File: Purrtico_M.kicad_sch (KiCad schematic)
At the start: 119 parts, among them J1 Conn_02x05_Odd_Even, J2 Conn_01x02, J4 Conn_01x02, U1 OPA1679, U2 OPA1679, U3 OPA1679

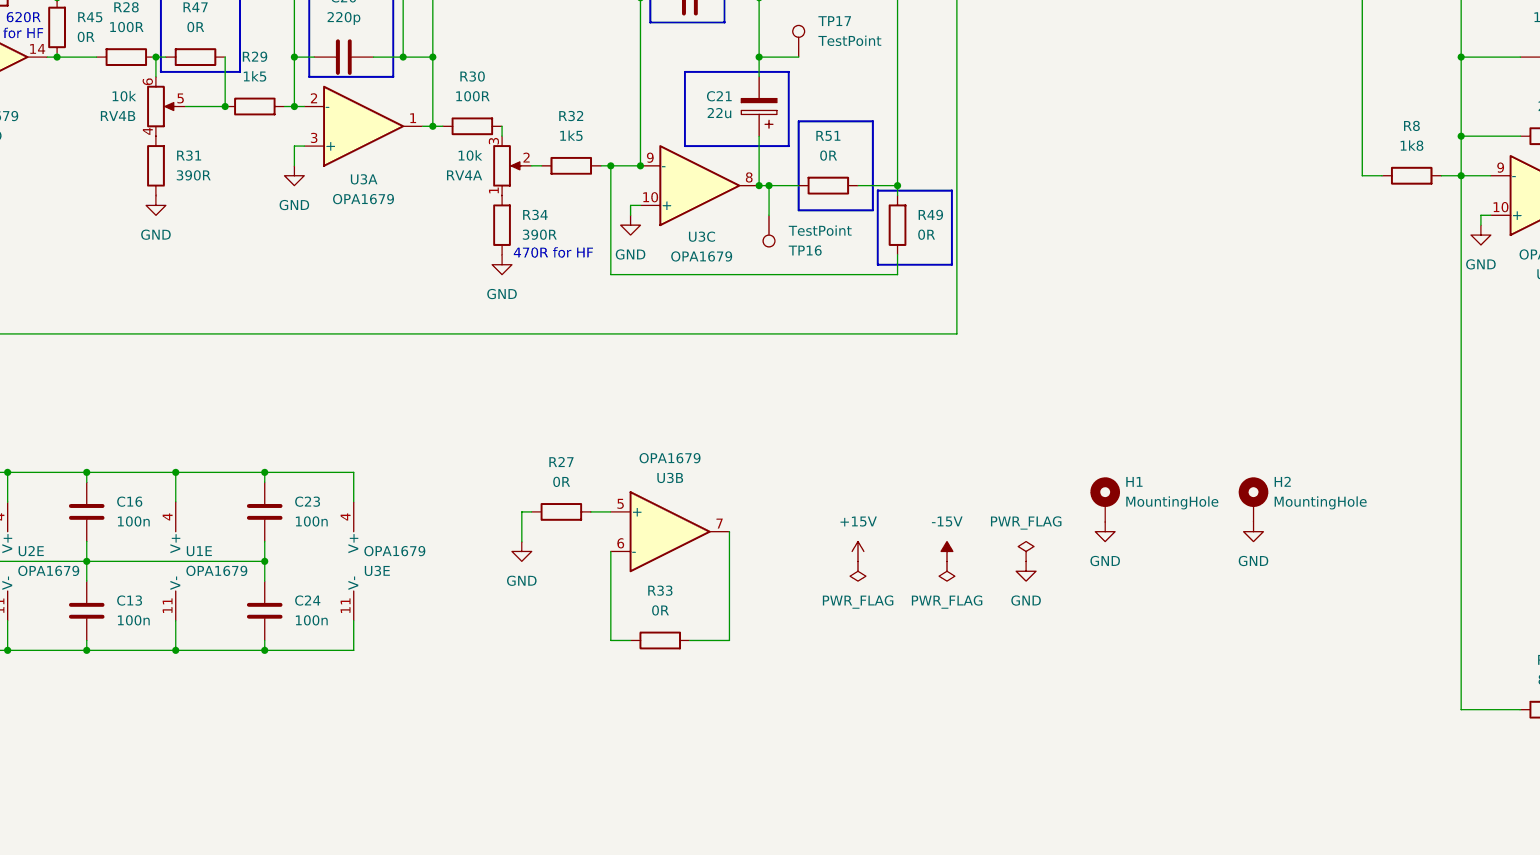
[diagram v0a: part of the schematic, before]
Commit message: added input gain control
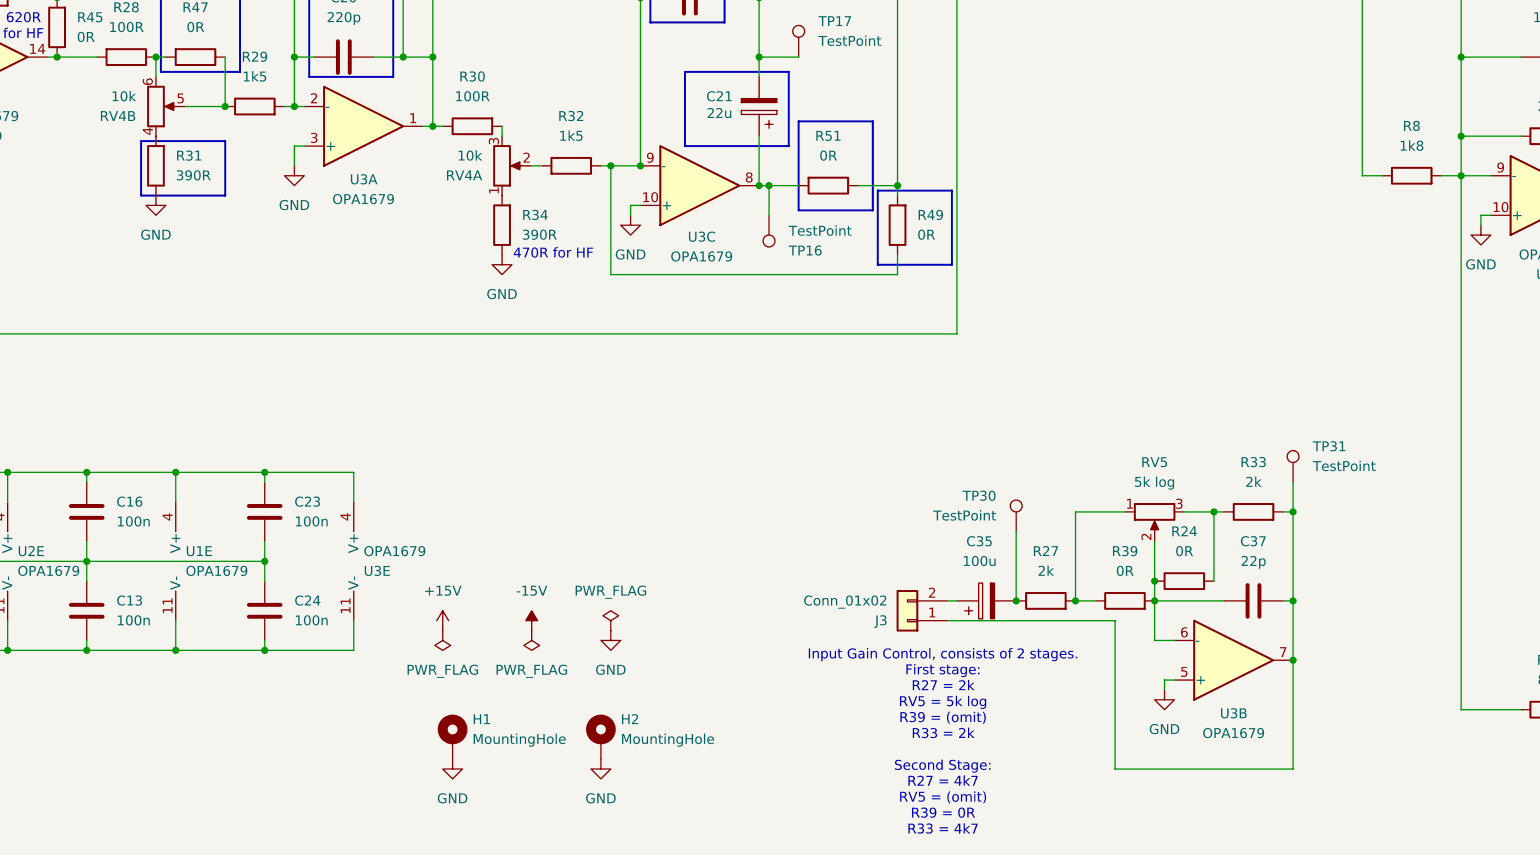
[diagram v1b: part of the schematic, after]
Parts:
- added C35: 100u, Capacitor_THT:CP_Radial_D6.3mm_P2.50mm, symbol Device:C_Polarized
- added C37: 22p, Capacitor_SMD:C_1206_3216Metric, symbol Device:C
- added J3: Conn_01x02, Connector_PinHeader_2.54mm:PinHeader_1x02_P2.54mm_Vertical, symbol Connector_Generic:Conn_01x02
- added R24, R39: 0R, Resistor_SMD:R_1206_3216Metric, symbol Device:R
- added RV5: 5k log, Connector_PinHeader_2.54mm:PinHeader_1x03_P2.54mm_Vertical, symbol Device:R_Potentiometer
- added TP30, TP31: TestPoint, TestPoint:TestPoint_THTPad_D1.0mm_Drill0.5mm, symbol Connector:TestPoint
- R27, R33: value 0R -> 2k
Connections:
- net GND: now also U3.5 (+); no longer R27.1
- net at R27.2: now also R39.1, RV5.1; no longer U3.5 (+)
- net at U3.6 (-): now also C37.2, R24.1, R39.2, RV5.2; no longer R33.1
- net at R33.2, U3.7: now also C37.1, J3.1 (Pin_1), TP31.1
- new net: R24.2, R33.1, RV5.3
- new net: C35.2, R27.1, TP30.1
- new net: C35.1, J3.2 (Pin_2)
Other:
- note added: "Input Gain Control, consists of 2 stages. First stage: R27 = 2k RV5 = 5k log R39 = (omit) R33 = 2k Second Stage: R27 = 4k7 RV5 = (omit) R39 = 0R R33 = 4k7"
- moved on the sheet: H1, H2, R27, R33, U3B

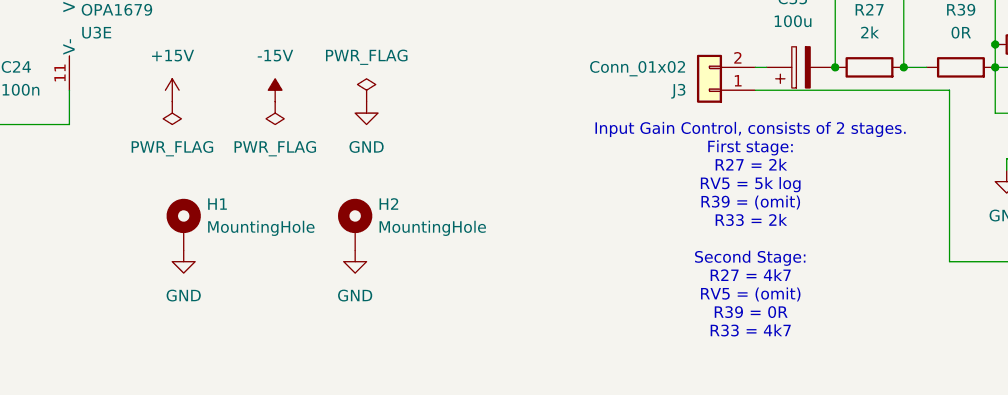
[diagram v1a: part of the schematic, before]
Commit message: added 0R for mounting holes
as well as some small layout refinements
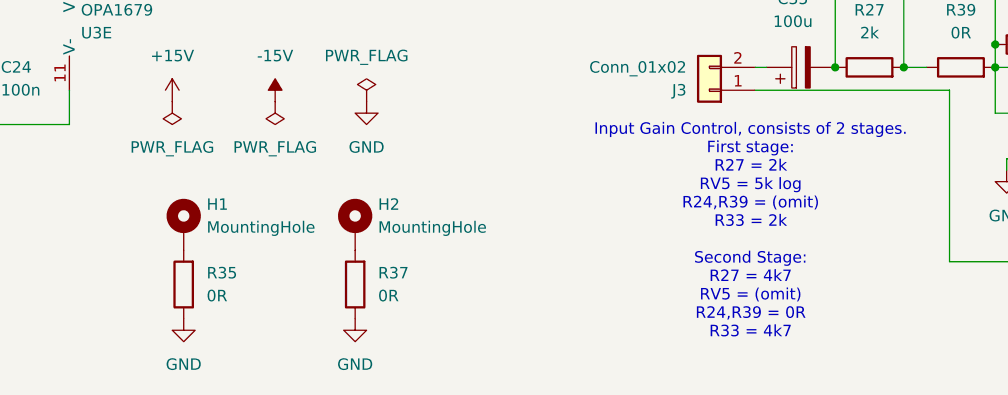
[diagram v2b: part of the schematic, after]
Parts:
- added R35, R37: 0R, Resistor_SMD:R_1206_3216Metric, symbol Device:R
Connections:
- net GND: now also R35.1, R37.1; no longer H1.1, H2.1
- new net: H2.1, R37.2
- new net: H1.1, R35.2
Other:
- note added: "Input Gain Control, consists of 2 stages. First stage: R27 = 2k RV5 = 5k log R24,R39 = (omit) R33 = 2k Second Stage: R27 = 4k7 RV5 = (omit) R24,R39 = 0R R33 = 4k7"
- note removed: "Input Gain Control, consists of 2 stages. First stage: R27 = 2k RV5 = 5k log R39 = (omit) R33 = 2k Second Stage: R27 = 4k7 RV5 = (omit) R39 = 0R R33 = 4k7"
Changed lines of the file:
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@@
 	(title_block
 		(title "Purrtico M")
-		(date "2024-08-06")
+		(date "2024-08-14")
 		(rev "01")
 		(company "Greybox Audio")
@@
 		)
 	)
-	(text "Input Gain Control, consists of 2 stages.\nFirst stage:\nR27 = 2k\nRV5 = 5k log\nR39 = (omit)\nR33 = 2k\n\nSecond Stage:\nR27 = 4k7\nRV5 = (omit)\nR39 = 0R\nR33 = 4k7"
+	(text "Input Gain Control, consists of 2 stages.\nFirst stage:\nR27 = 2k\nRV5 = 5k log\nR24,R39 = (omit)\nR33 = 2k\n\nSecond Stage:\nR27 = 4k7\nRV5 = (omit)\nR24,R39 = 0R\nR33 = 4k7"
 		(exclude_from_sim no)
 		(at 212.852 210.058 0)
@@
 	)
 	(symbol
+		(lib_id "Device:R")
+		(at 149.86 215.9 180)
+		(unit 1)
+		(exclude_from_sim no)
+		(in_bom yes)
+		(on_board yes)
+		(dnp no)
+		(fields_autoplaced yes)
+		(property "Reference" "R35"
+			(at 152.4 214.6299 0)
+			(effects
+				(font
+					(size 1.27 1.27)
+				)
+				(justify right)
+			)
+		)
+		(property "Value" "0R"
+			(at 152.4 217.1699 0)
+			(effects
+				(font
+					(size 1.27 1.27)
+				)
+				(justify right)
+			)
+		)
+		(property "Footprint" "Resistor_SMD:R_1206_3216Metric"
+			(at 151.638 215.9 90)
+			(effects
+				(font
+					(size 1.27 1.27)
+				)
+				(hide yes)
+			)
+		)
+		(property "Datasheet" "~"
+			(at 149.86 215.9 0)
+			(effects
+				(font
+					(size 1.27 1.27)
+				)
+				(hide yes)
+			)
+		)
+		(property "Description" "Resistor"
+			(at 149.86 215.9 0)
+			(effects
+				(font
+					(size 1.27 1.27)
+				)
+				(hide yes)
+			)
+		)
+		(pin "2"
+		)
+		(pin "1"
+		)
+		(instances
+			(project "Purrtico_M"
+				(path "/a0898129-0e9a-4d09-a24b-7ec1243d6ca2"
+					(reference "R35")
+					(unit 1)
+				)
+			)
+		)
+	)
+	(symbol
 		(lib_id "Device:C")
 		(at 177.8 44.45 90)
@@
 	(symbol
 		(lib_id "Device:R")
+		(at 168.91 215.9 180)
+		(unit 1)
+		(exclude_from_sim no)
+		(in_bom yes)
+		(on_board yes)
+		(dnp no)
+		(fields_autoplaced yes)
+		(property "Reference" "R37"
+			(at 171.45 214.6299 0)
+			(effects
+				(font
+					(size 1.27 1.27)
+				)
+				(justify right)
+			)
+		)
+		(property "Value" "0R"
+			(at 171.45 217.1699 0)
+			(effects
+				(font
+					(size 1.27 1.27)
+				)
+				(justify right)
+			)
+		)
+		(property "Footprint" "Resistor_SMD:R_1206_3216Metric"
+			(at 170.688 215.9 90)
+			(effects
+				(font
+					(size 1.27 1.27)
+				)
+				(hide yes)
+			)
+		)
+		(property "Datasheet" "~"
+			(at 168.91 215.9 0)
+			(effects
+				(font
+					(size 1.27 1.27)
+				)
+				(hide yes)
+			)
+		)
+		(property "Description" "Resistor"
+			(at 168.91 215.9 0)
+			(effects
+				(font
+					(size 1.27 1.27)
+				)
+				(hide yes)
+			)
+		)
+		(pin "2"
+		)
+		(pin "1"
+		)
+		(instances
+			(project "Purrtico_M"
+				(path "/a0898129-0e9a-4d09-a24b-7ec1243d6ca2"
+					(reference "R37")
+					(unit 1)
+				)
+			)
+		)
+	)
+	(symbol
+		(lib_id "Device:R")
 		(at 337.82 59.69 90)
 		(unit 1)
@@
 		(lib_name "GND_1")
 		(lib_id "power:GND")
-		(at 149.86 212.09 0)
+		(at 149.86 219.71 0)
 		(unit 1)
 		(exclude_from_sim no)
@@
 		(fields_autoplaced yes)
 		(property "Reference" "#PWR011"
-			(at 149.86 218.44 0)
+			(at 149.86 226.06 0)
 			(effects
 				(font
@@
 		)
 		(property "Value" "GND"
-			(at 149.86 217.17 0)
+			(at 149.86 224.79 0)
 			(effects
 				(font
@@
 		)
 		(property "Footprint" ""
-			(at 149.86 212.09 0)
+			(at 149.86 219.71 0)
 			(effects
 				(font
@@
 		)
 		(property "Datasheet" ""
-			(at 149.86 212.09 0)
+			(at 149.86 219.71 0)
 			(effects
 				(font
@@
 		)
 		(property "Description" "Power symbol creates a global label with name \"GND\" , ground"
-			(at 149.86 212.09 0)
+			(at 149.86 219.71 0)
 			(effects
 				(font
@@
 		(lib_name "GND_1")
 		(lib_id "power:GND")
-		(at 168.91 212.09 0)
+		(at 168.91 219.71 0)
 		(unit 1)
 		(exclude_from_sim no)
@@
 		(fields_autoplaced yes)
 		(property "Reference" "#PWR012"
-			(at 168.91 218.44 0)
+			(at 168.91 226.06 0)
 			(effects
 				(font
@@
 		)
 		(property "Value" "GND"
-			(at 168.91 217.17 0)
+			(at 168.91 224.79 0)
 			(effects
 				(font
@@
 		)
 		(property "Footprint" ""
-			(at 168.91 212.09 0)
+			(at 168.91 219.71 0)
 			(effects
 				(font
@@
 		)
 		(property "Datasheet" ""
-			(at 168.91 212.09 0)
+			(at 168.91 219.71 0)
 			(effects
 				(font
@@
 		)
 		(property "Description" "Power symbol creates a global label with name \"GND\" , ground"
-			(at 168.91 212.09 0)
+			(at 168.91 219.71 0)
 			(effects
 				(font

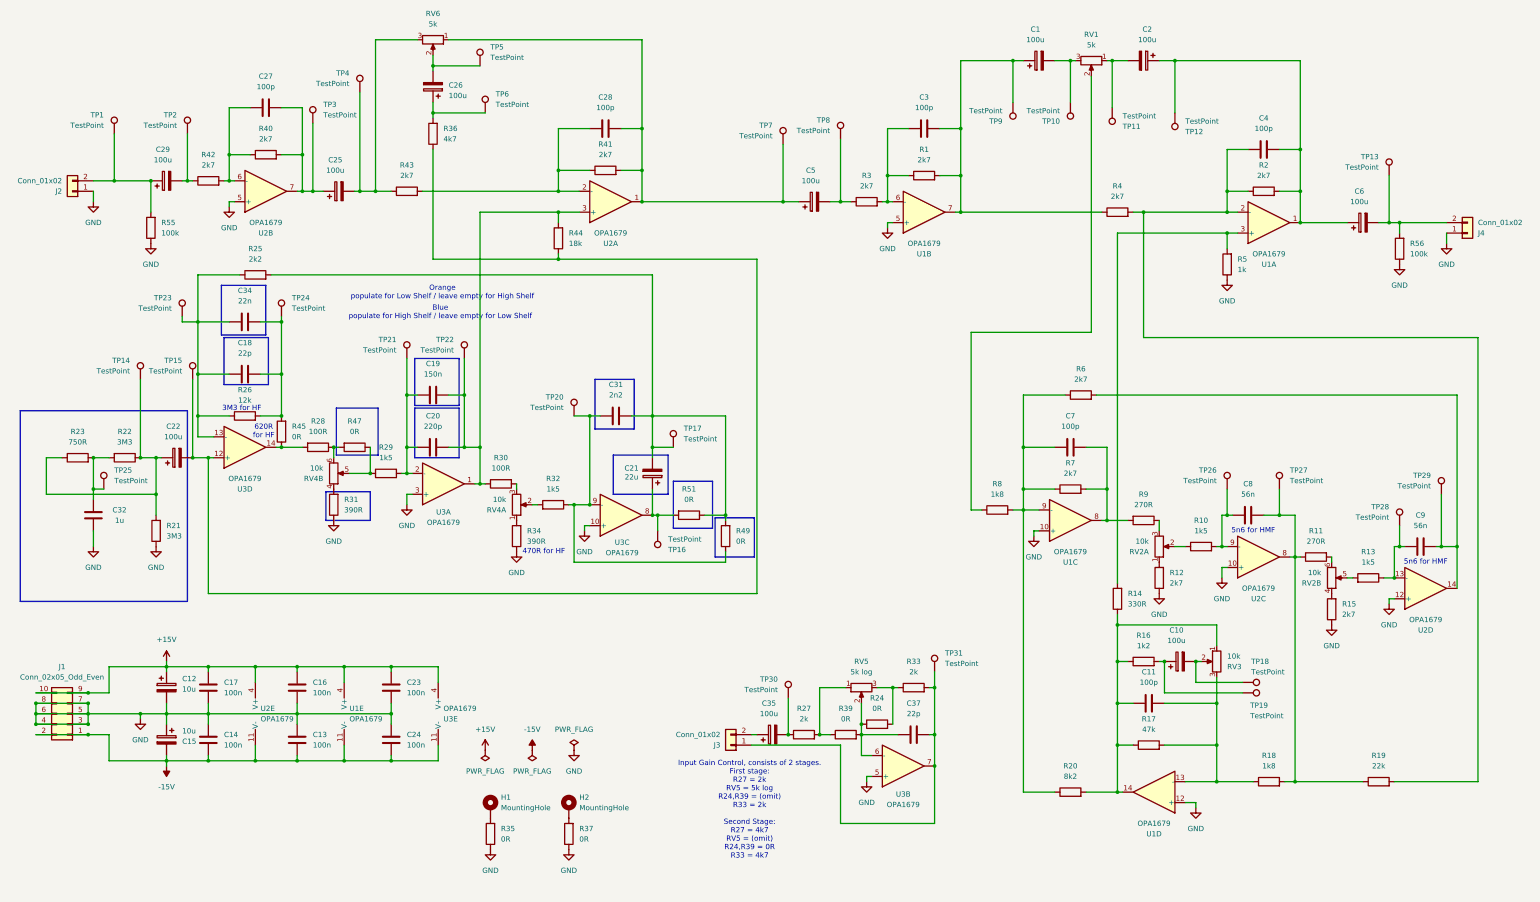
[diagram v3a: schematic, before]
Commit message: update potentiometer values
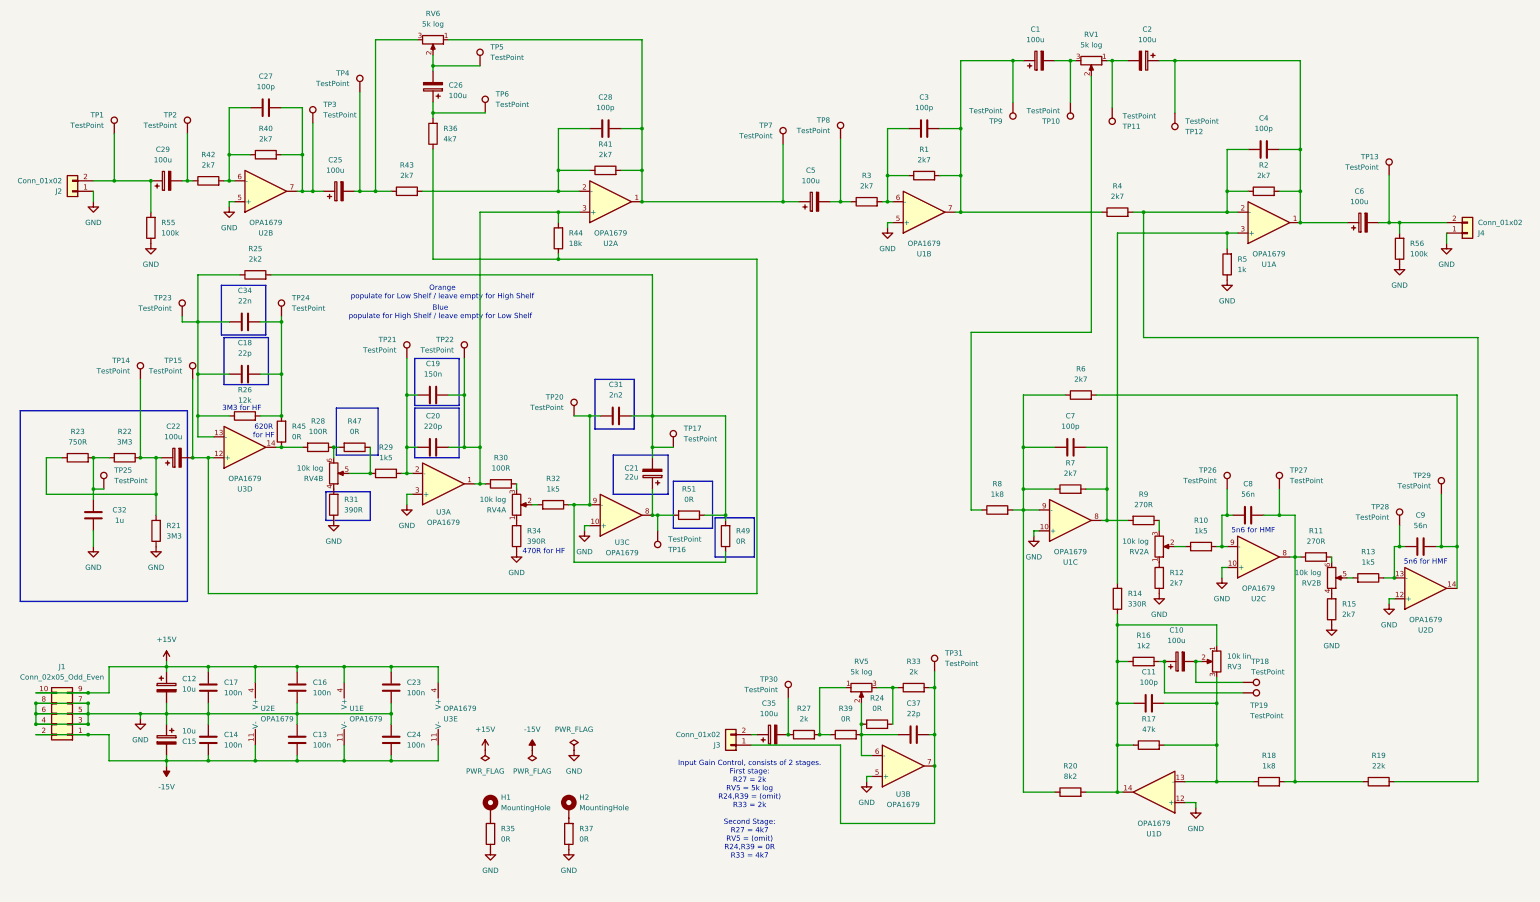
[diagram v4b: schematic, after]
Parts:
- RV1, RV6: value 5k -> 5k log
- RV2, RV4: value 10k -> 10k log
- RV3: value 10k -> 10k lin
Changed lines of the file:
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@@
 			)
 		)
-		(property "Value" "5k"
+		(property "Value" "5k log"
 			(at 295.91 24.13 90)
 			(effects
@@
 			)
 		)
-		(property "Value" "5k"
+		(property "Value" "5k log"
 			(at 135.89 19.05 90)
 			(effects
@@
 			)
 		)
-		(property "Value" "10k"
+		(property "Value" "10k log"
 			(at 109.22 127.0001 0)
 			(effects
@@
 			)
 		)
-		(property "Value" "10k"
+		(property "Value" "10k log"
 			(at 309.88 144.7801 0)
 			(effects
@@
 			)
 		)
-		(property "Value" "10k"
+		(property "Value" "10k log"
 			(at 351.79 152.4001 0)
 			(effects
@@
 			)
 		)
-		(property "Value" "10k"
+		(property "Value" "10k log"
 			(at 153.67 134.6201 0)
 			(effects
@@
 			)
 		)
-		(property "Value" "10k"
+		(property "Value" "10k lin"
 			(at 328.93 172.7201 0)
 			(effects

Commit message: added gerber files
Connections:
- net at R27.2, R39.1: now also RV5.3; no longer RV5.1
- net at R24.2, R33.1: now also RV5.1; no longer RV5.3
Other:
- moved on the sheet: RV5
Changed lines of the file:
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@@
 	(title_block
 		(title "Purrtico M")
-		(date "2024-08-15")
+		(date "2024-08-16")
 		(rev "01")
 		(company "Greybox Audio")
@@
 	(symbol
 		(lib_id "Device:R_Potentiometer")
-		(at 240.03 180.34 90)
-		(mirror x)
+		(at 240.03 180.34 270)
 		(unit 1)
 		(exclude_from_sim no)

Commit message: updated comments
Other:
- note added: "Blue populate for High Shelf / omit for Low Shelf"
- note added: "Important! Only connect a single mounting hole to ground and omit the other 0R resistor!"
- note added: "Input Gain Control, consists of 2 stages. First stage: R27,R33 = 2k RV5 = 5k log R24,R39 = (omit) Second Stage: R27,R33 = 4k7 RV5 = (omit) R24,R39 = 0R"
- note added: "Orange populate for Low Shelf / omit for High Shelf"
- note removed: "Blue populate for High Shelf / leave empty for Low Shelf"
- note removed: "Input Gain Control, consists of 2 stages. First stage: R27 = 2k RV5 = 5k log R24,R39 = (omit) R33 = 2k Second Stage: R27 = 4k7 RV5 = (omit) R24,R39 = 0R R33 = 4k7"
- note removed: "Orange populate for Low Shelf / leave empty for High Shelf"
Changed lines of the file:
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@@
 	(title_block
 		(title "Purrtico M")
-		(date "2024-08-16")
+		(date "2025-01-19")
 		(rev "01")
 		(company "Greybox Audio")
@@
 		)
 	)
-	(text "Input Gain Control, consists of 2 stages.\nFirst stage:\nR27 = 2k\nRV5 = 5k log\nR24,R39 = (omit)\nR33 = 2k\n\nSecond Stage:\nR27 = 4k7\nRV5 = (omit)\nR24,R39 = 0R\nR33 = 4k7"
+	(text "Important!\nOnly connect a single mounting hole to ground and omit the other 0R resistor!"
+		(exclude_from_sim no)
+		(at 159.004 228.346 0)
+		(effects
+			(font
+				(size 1.27 1.27)
+			)
+		)
+	)
+	(text "Input Gain Control, consists of 2 stages.\nFirst stage:\nR27,R33 = 2k\nRV5 = 5k log\nR24,R39 = (omit)\n\nSecond Stage:\nR27,R33 = 4k7\nRV5 = (omit)\nR24,R39 = 0R"
 		(exclude_from_sim no)
 		(at 212.852 210.058 0)
@@
 		)
 	)
-	(text "Orange\npopulate for Low Shelf / leave empty for High Shelf"
+	(text "Orange\npopulate for Low Shelf / omit for High Shelf"
 		(exclude_from_sim no)
 		(at 138.176 84.328 0)
@@
 		)
 	)
-	(text "Blue\npopulate for High Shelf / leave empty for Low Shelf"
+	(text "Blue\npopulate for High Shelf / omit for Low Shelf"
 		(exclude_from_sim no)
 		(at 137.668 89.154 0)
